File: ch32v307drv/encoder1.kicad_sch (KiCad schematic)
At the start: 11 parts, among them J8 AJT65B8813, U4 AM26LV32xD

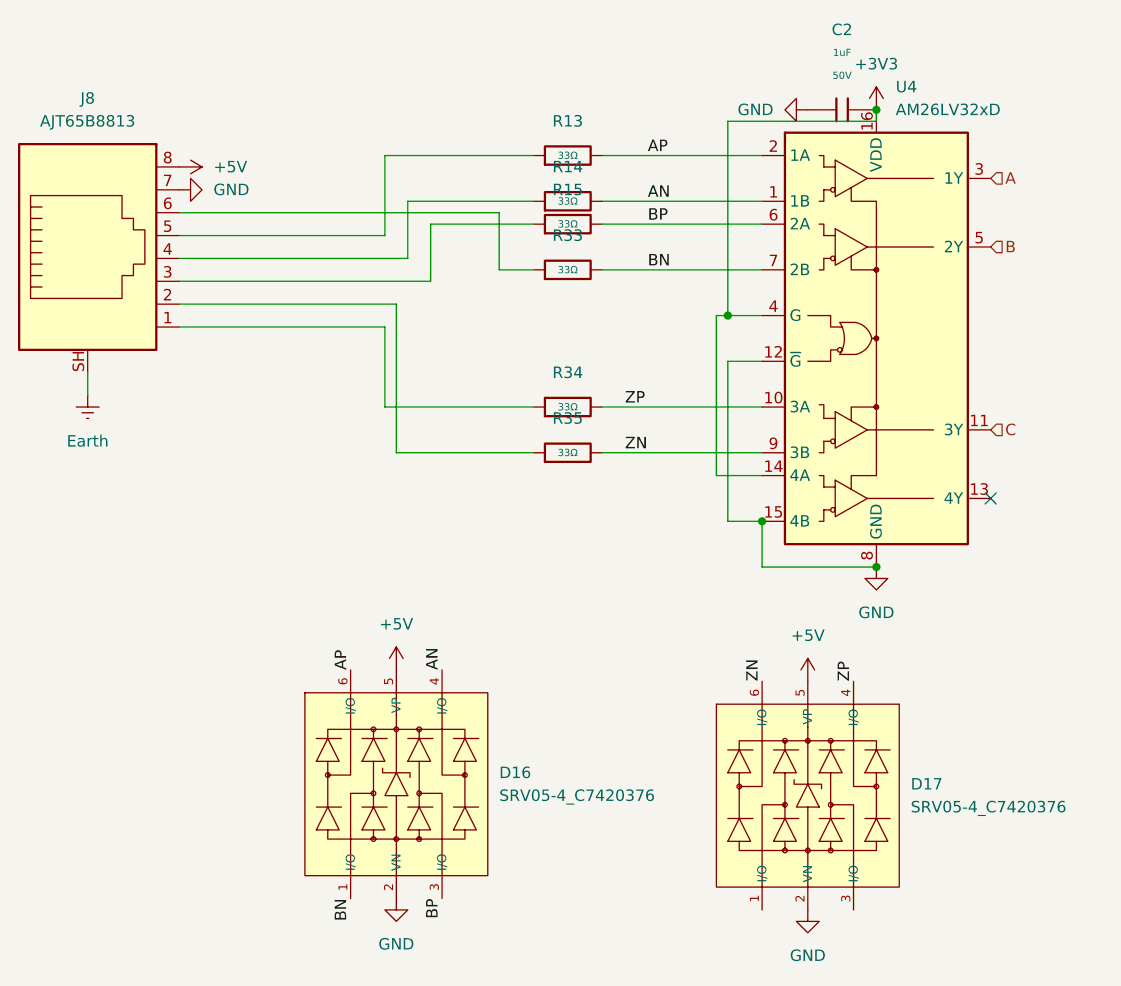
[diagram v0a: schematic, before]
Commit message: add rs-422 termination resistors
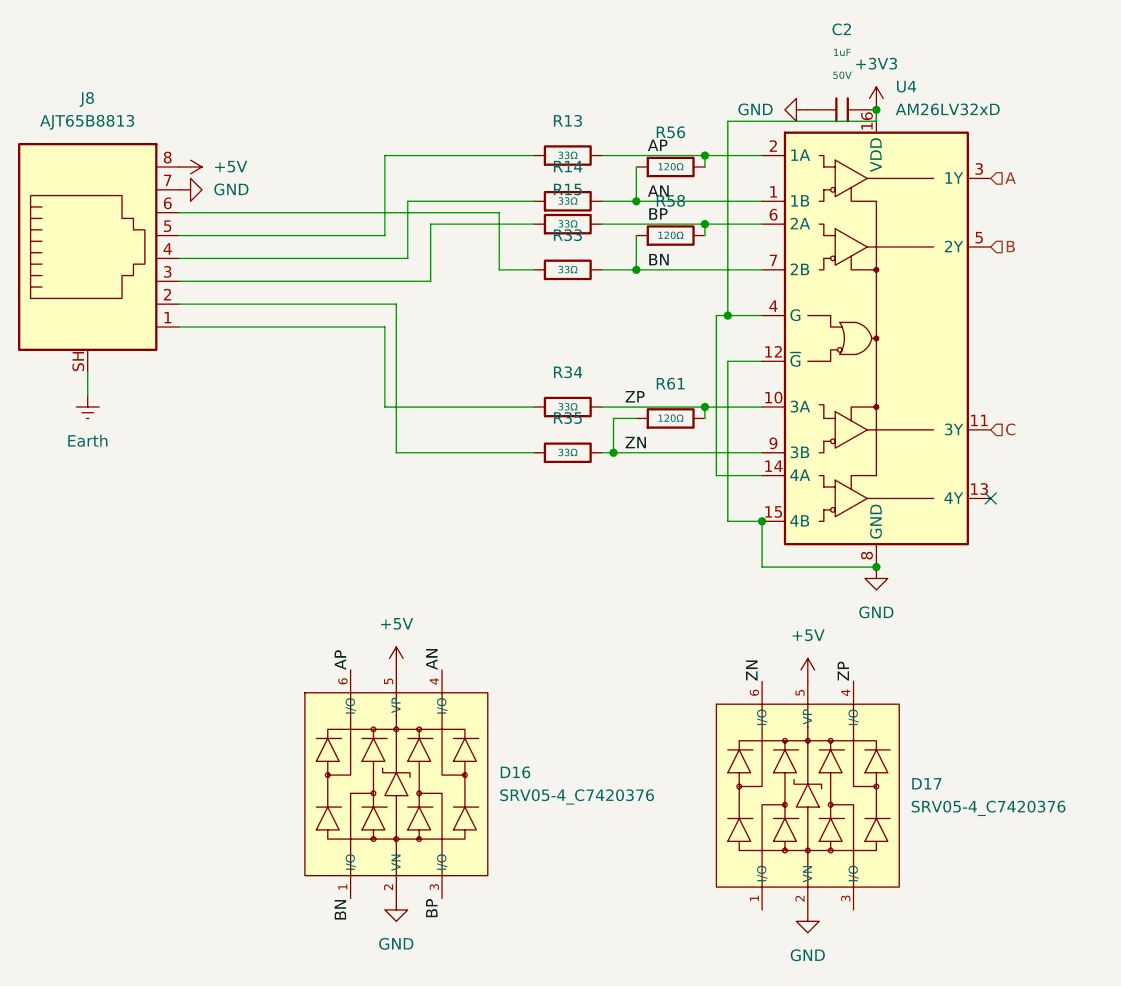
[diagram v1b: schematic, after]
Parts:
- added R56, R58, R61: 120Ω, PCM_JLCPCB:R_0603, symbol PCM_JLCPCB-Resistors:0603,120Ω
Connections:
- net AN: now also R56.1
- net AP: now also R56.2
- net BN: now also R58.1
- net BP: now also R58.2
- net ZN: now also R61.1
- net ZP: now also R61.2
